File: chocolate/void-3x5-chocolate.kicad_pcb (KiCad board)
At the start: 2 copper layers, 140.5 x 112.5 mm, 81 parts, among them J1 Conn_01x02, J2 Conn_01x03_MountingPin, J3 Conn_01x02

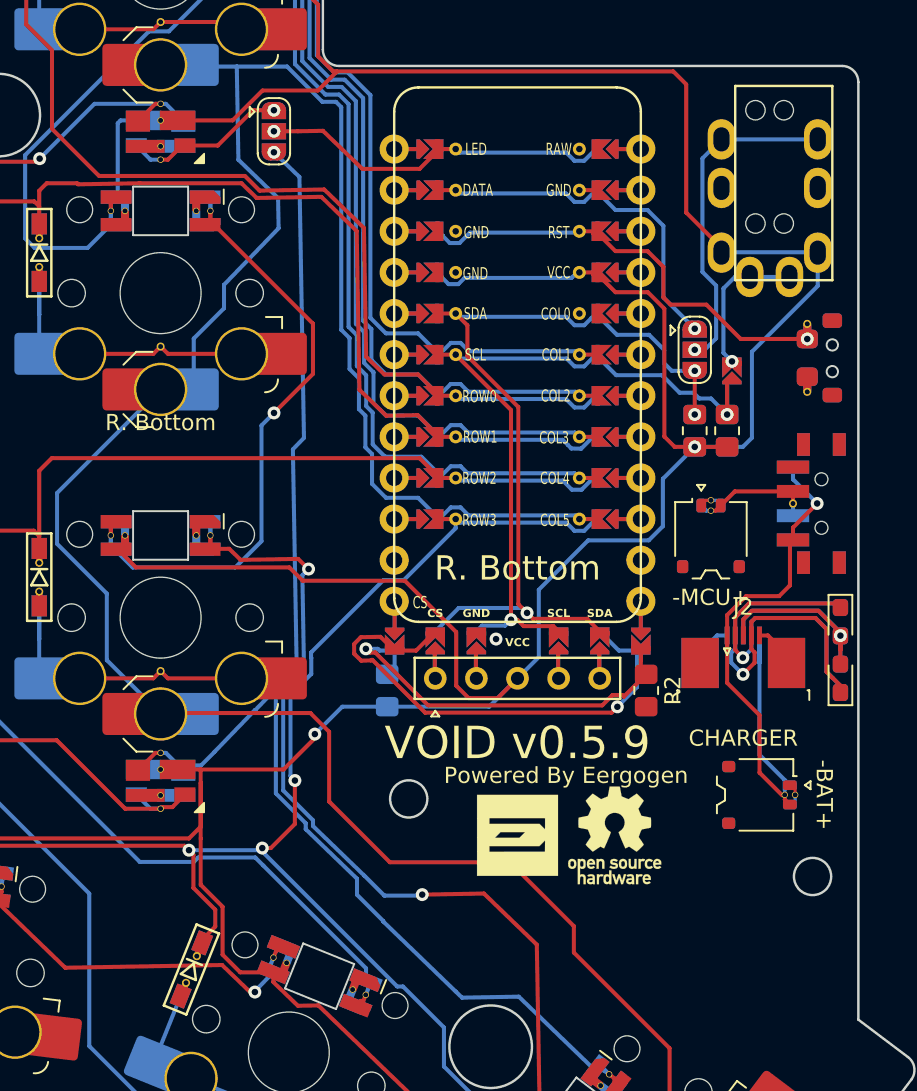
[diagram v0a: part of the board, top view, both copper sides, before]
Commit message: usb-c mod for hybrid
* updated
  - submodule
  - ergogen yaml
  - schematic and pcb
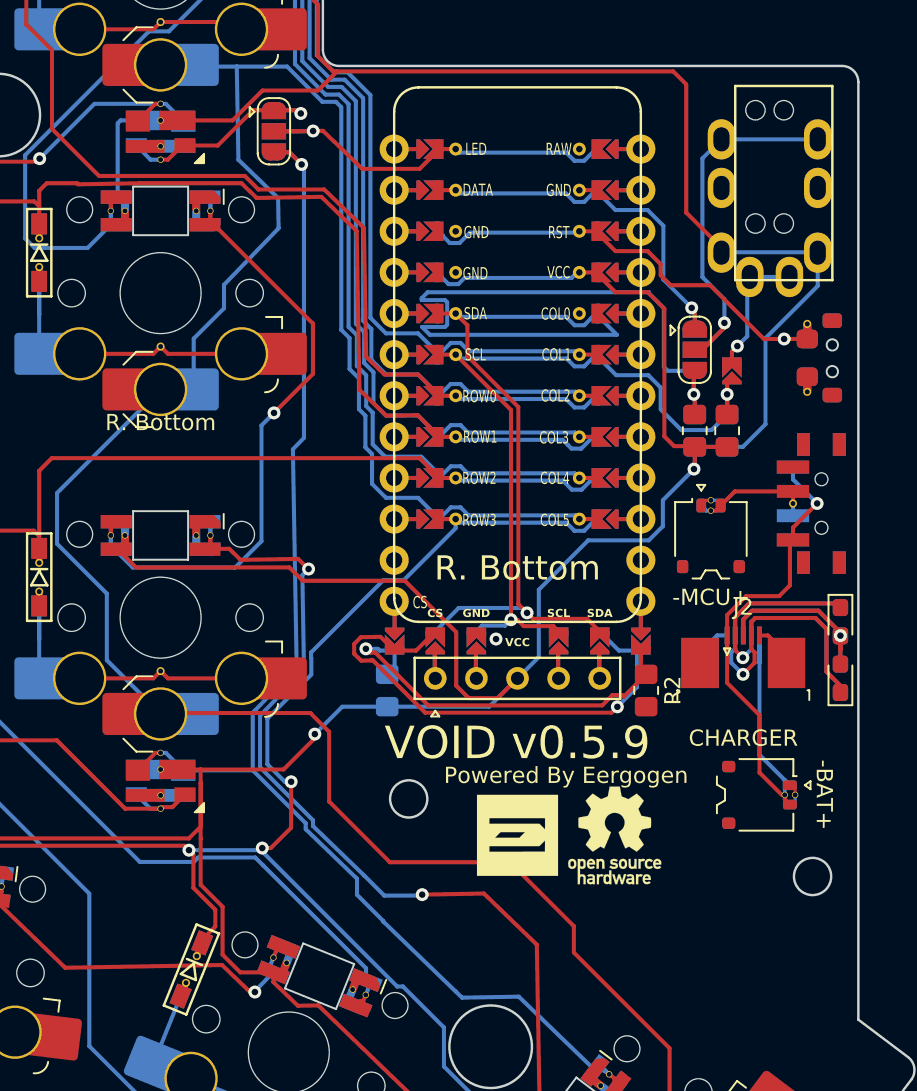
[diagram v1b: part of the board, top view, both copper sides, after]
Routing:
- net SDA: track 52.7 -> 87.5 mm, vias 3 -> 2
- net Net-(JP2-C): track 20.1 -> 23.7 mm
- net LED_UNDERGLOW: track 10.1 -> 13.6 mm
- net SCL: track 48.2 -> 51.0 mm
- net LED: track 21.9 -> 24.4 mm
- net LED_PER_KEY: track 83.4 -> 81.8 mm
- net DATA: track 22.5 -> 23.9 mm
- net VCC: track 618.5 -> 619.8 mm
- net row_thumb: track 104.5 -> 105.7 mm
- net Net-(L13-DIN): track 55.9 -> 57.0 mm

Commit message: updated choc
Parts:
- removed TRRS1: MJ-4PP-9, TB2086_MISC:TRRS-PJ-320A-rev
- added J4: Conn_01x03, TB2086_MISC:Pogopin_1x03_P2.54mm, F.Cu at (212.8, 108.0)
- added SW_SPDT2: SW_SPDT2, TB2086_SMD:SW_SPDT_PCM12, F.Cu at (217.2, 87.5)
- J1: value Conn_01x02 -> USB_C_Receptacle_PowerOnly_6P; footprint TB2086_SMD:Molex_Pico-EZmate_78171-0002_1x02-1MP_P1.20mm_Vertical_rev -> TB2086_SMD:USB-20C-F-6C16_rev
- J2: value Conn_01x03_MountingPin -> Conn_01x02; footprint TB2086_SMD:TE_0-1734839-5_1x05-1MP_P0.5mm_Horizontal_rev -> TB2086_SMD:JST_PH_S2B-PH-SM4-TB_1x02-1MP_P2.00mm_Horizontal_rev
- J3: footprint TB2086_SMD:Molex_Pico-EZmate_78171-0002_1x02-1MP_P1.20mm_Vertical_rev -> TB2086_MISC:Pogopin_1x02_P2.54mm
- LED2, LED3: moved to F.Cu
- SW_SPDT1: value SW_SPDT -> SW_SPDT1; footprint TB2086_SMD:SW_SPDT_PCM12_reversible -> TB2086_SMD:SW_SPDT_PCM12
- moved J1 22.7 mm to (216.4, 69.5), turned to 90 degrees
- moved J3 17.5 mm to (212.6, 90.0)
- moved LED1 5.50 mm to (218.8, 94.8), turned to -90 degrees
- moved LED2 2.00 mm to (218.8, 94.8), turned to 90 degrees
- moved LED3 2.00 mm to (218.8, 98.3)
- moved SW_SPDT1 2.00 mm to (217.2, 87.5)
- moved LED4 1.50 mm to (218.8, 98.3)
- moved RSW1 1.00 mm to (218.2, 79.5)
- moved J2 0.15 mm to (212.8, 99.0)
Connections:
- J2 pad 1: BAT -> GND
- JP2 pad 2: Net-(JP2-C) -> Net-(J1-CC2)
- JP3 pad 2: Net-(JP3-B) -> Net-(J1-CC1)
- LED1 pad 1: Net-(J2-Pin_4) -> Net-(J4-Pin_1)
- LED1 pad 2: Net-(J2-Pin_3) -> Net-(J4-Pin_2)
- LED2 pad 1: Net-(J2-Pin_4) -> Net-(J4-Pin_1)
- LED2 pad 2: Net-(J2-Pin_3) -> Net-(J4-Pin_2)
- LED3 pad 1: Net-(J2-Pin_2) -> Net-(J4-Pin_3)
- LED3 pad 2: Net-(J2-Pin_3) -> Net-(J4-Pin_2)
- LED4 pad 1: Net-(J2-Pin_2) -> Net-(J4-Pin_3)
- LED4 pad 2: Net-(J2-Pin_3) -> Net-(J4-Pin_2)
- SW_SPDT1 pad 2: Net-(J1-Pin_2) -> Net-(J2-Pin_2)
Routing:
- net Net-(J4-Pin_1): track 0.00 -> 37.2 mm
- net Net-(J4-Pin_2): track 0.00 -> 32.0 mm
- net BAT: track 39.2 -> 7.60 mm, vias 1 -> 0
- net SDA: track 87.5 -> 58.3 mm
- net Net-(J4-Pin_3): track 0.00 -> 29.1 mm
- net Net-(JP2-C): track 23.7 -> 0.00 mm, vias 1 -> 0
- net Net-(J2-Pin_4): track 23.2 -> 0.00 mm, vias 1 -> 0
- net Net-(J1-CC2): track 0.00 -> 21.1 mm, vias 0 -> 2
- net Net-(J2-Pin_3): track 20.9 -> 0.00 mm, vias 1 -> 0
- net Net-(J1-CC1): track 0.00 -> 17.7 mm, vias 0 -> 3
- net Net-(JP3-B): track 9.21 -> 0.00 mm, vias 1 -> 0
- net Net-(J1-Pin_2): track 7.23 -> 0.00 mm
- net GND: track 5.26 -> 1.01 mm, vias 1 -> 2
- net VCC: track 619.8 -> 623.9 mm, vias 5 -> 7
- net RESET: track 28.1 -> 25.8 mm, vias 1 -> 0
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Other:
- outline, holes or cut-outs redrawn
- board text added: "- +"
- board text added: "VOID v0.6.0"
- board text removed: "-BAT+"
- board text removed: "CHARGER"
- board text removed: "VOID v0.5.9"

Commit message: updated choc
* fixed corner
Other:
- board text added: "This corner was manually created."
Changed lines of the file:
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@@
 		)
 		(pad "1" thru_hole circle
-			(at -2.200002 0 353)
+			(at -2.200003 0 353)
 			(size 0.4 0.4)
 			(drill 0.3)
@@
 		)
 		(pad "3" thru_hole circle
-			(at 2.200002 0 353)
+			(at 2.200003 0 353)
 			(size 0.4 0.4)
 			(drill 0.3)
@@
 		(fp_arc
 			(start -6.95 -6.45)
-			(mid -6.803555 -6.803554)
+			(mid -6.803554 -6.803555)
 			(end -6.45 -6.95)
 			(stroke
@@
 		(fp_arc
 			(start -6.45 6.95)
-			(mid -6.803554 6.803555)
+			(mid -6.803555 6.803554)
 			(end -6.95 6.45)
 			(stroke
@@
 		(fp_arc
 			(start -3.45 6.125001)
-			(mid -2.742893 6.417893)
+			(mid -2.742892 6.417892)
 			(end -2.45 7.125)
 			(stroke
@@
 		(fp_arc
 			(start -6.95 -6.45)
-			(mid -6.803555 -6.803554)
+			(mid -6.803554 -6.803555)
 			(end -6.45 -6.95)
 			(stroke
@@
 		(fp_arc
 			(start -6.45 6.95)
-			(mid -6.803554 6.803555)
+			(mid -6.803555 6.803554)
 			(end -6.95 6.45)
 			(stroke
@@
 		(fp_arc
 			(start -6.95 -6.45)
-			(mid -6.803555 -6.803554)
+			(mid -6.803554 -6.803555)
 			(end -6.45 -6.95)
 			(stroke
@@
 		(fp_arc
 			(start -6.45 6.95)
-			(mid -6.803554 6.803555)
+			(mid -6.803555 6.803554)
 			(end -6.95 6.45)
 			(stroke
@@
 		(fp_arc
 			(start -3.4 1.475)
-			(mid -2.826424 1.655849)
+			(mid -2.826425 1.655849)
 			(end -2.460307 2.13298)
 			(stroke
@@
 		(fp_arc
 			(start -0.299999 3.624999)
-			(mid -1.577272 3.167235)
+			(mid -1.577271 3.167235)
 			(end -2.455444 2.13293)
 			(stroke
@@
 		(fp_arc
 			(start 2.455444 2.13293)
-			(mid 1.577273 3.167237)
+			(mid 1.577274 3.167237)
 			(end 0.299999 3.624997)
 			(stroke
@@
 	(gr_arc
 		(start 188.052011 62.484287)
-		(mid 187.1 62.09)
+		(mid 187.100002 62.089998)
 		(end 186.705713 61.137989)
 		(stroke
@@
 		)
 	)
+	(gr_text "This corner was manually created. "
+		(at 187.69 61.3 0)
+		(layer "Cmts.User")
+		(effects
+			(font
+				(size 1 1)
+				(thickness 0.15)
+			)
+			(justify left bottom)
+		)
+	)

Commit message: updated PCBs
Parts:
- moved LED1 7.63 mm to (222.8, 101.3)
- moved LED2 7.63 mm to (222.8, 101.3)
- moved LED3 7.63 mm to (222.8, 104.8)
- moved LED4 7.63 mm to (222.8, 104.8)
- moved S17 7.63 mm to (188.6, 129.9)
- moved D1 7.63 mm to (94.2, 109.9)
- moved S3 7.63 mm to (97.7, 71.7)
- moved S16 7.63 mm to (167.2, 124.3)
- moved L3 7.63 mm to (97.2, 66.7)
- moved D10 7.63 mm to (153.1, 98.1)
- moved D11 7.63 mm to (153.1, 78.0)
- moved D13 7.63 mm to (173.2, 100.6)
- moved D14 7.63 mm to (173.2, 80.5)
- moved D17 7.63 mm to (182.6, 124.8)
- moved D4 7.63 mm to (113.0, 94.6)
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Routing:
- net Net-(L1-DOUT): track 37.5 -> 36.3 mm
- net col_index: track 201.3 -> 201.9 mm
- net Net-(L1-DIN): track 24.2 -> 23.5 mm
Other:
- outline, holes or cut-outs redrawn
- board text added: "Powered By Ergogen"
- board text added: "offset: 90, 70 from origin"
- board text removed: "Powered By Eergogen"
- board text removed: "This corner was manually created."
